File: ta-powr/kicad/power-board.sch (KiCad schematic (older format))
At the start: 7 parts, among them J1 PinSocket_16, J2 PinSocket_16, J3 PinSocket_4, J4 PinSocket_4, J5 PinSocket_4, J6 PinSocket_4, J7 MountingHole

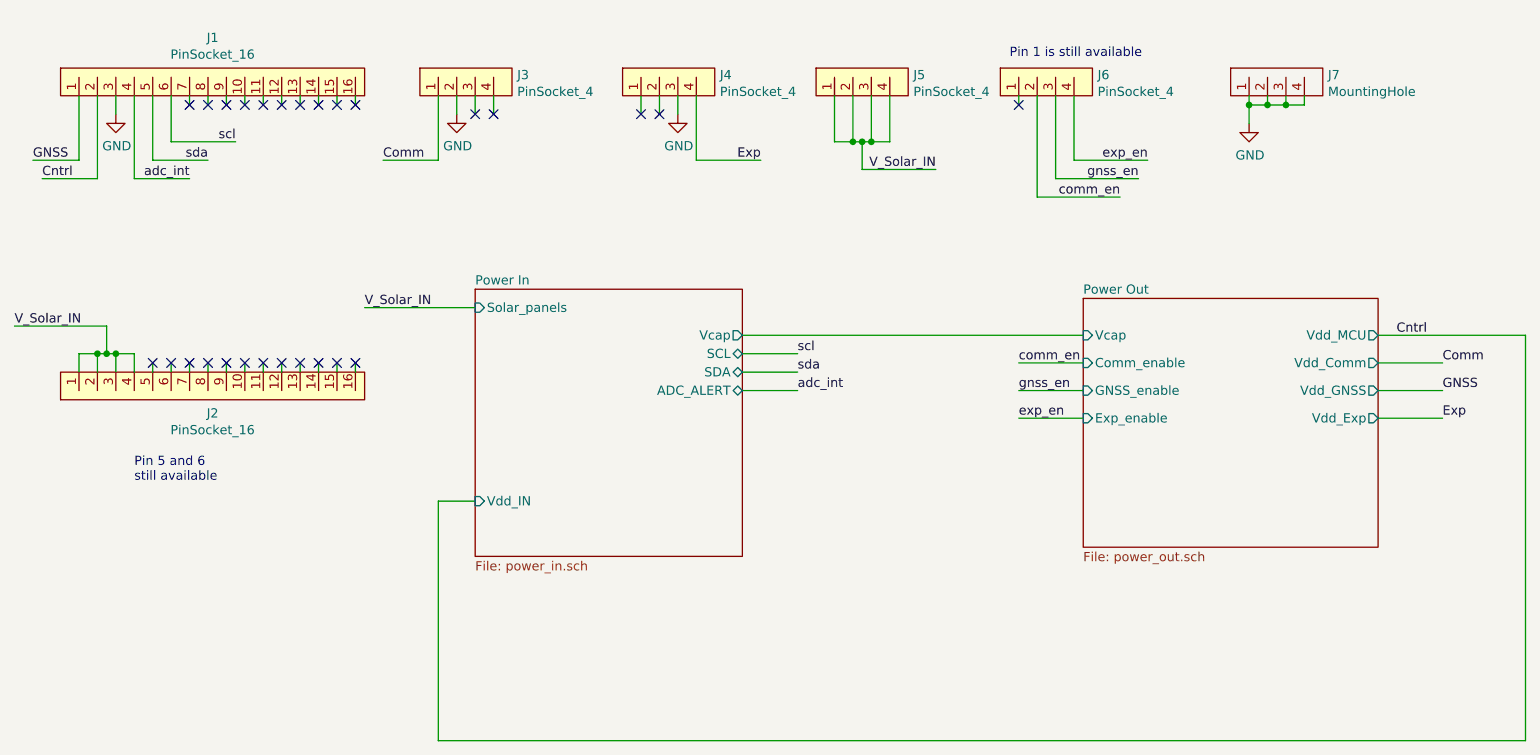
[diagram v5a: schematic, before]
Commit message: layout redone after pinout changes
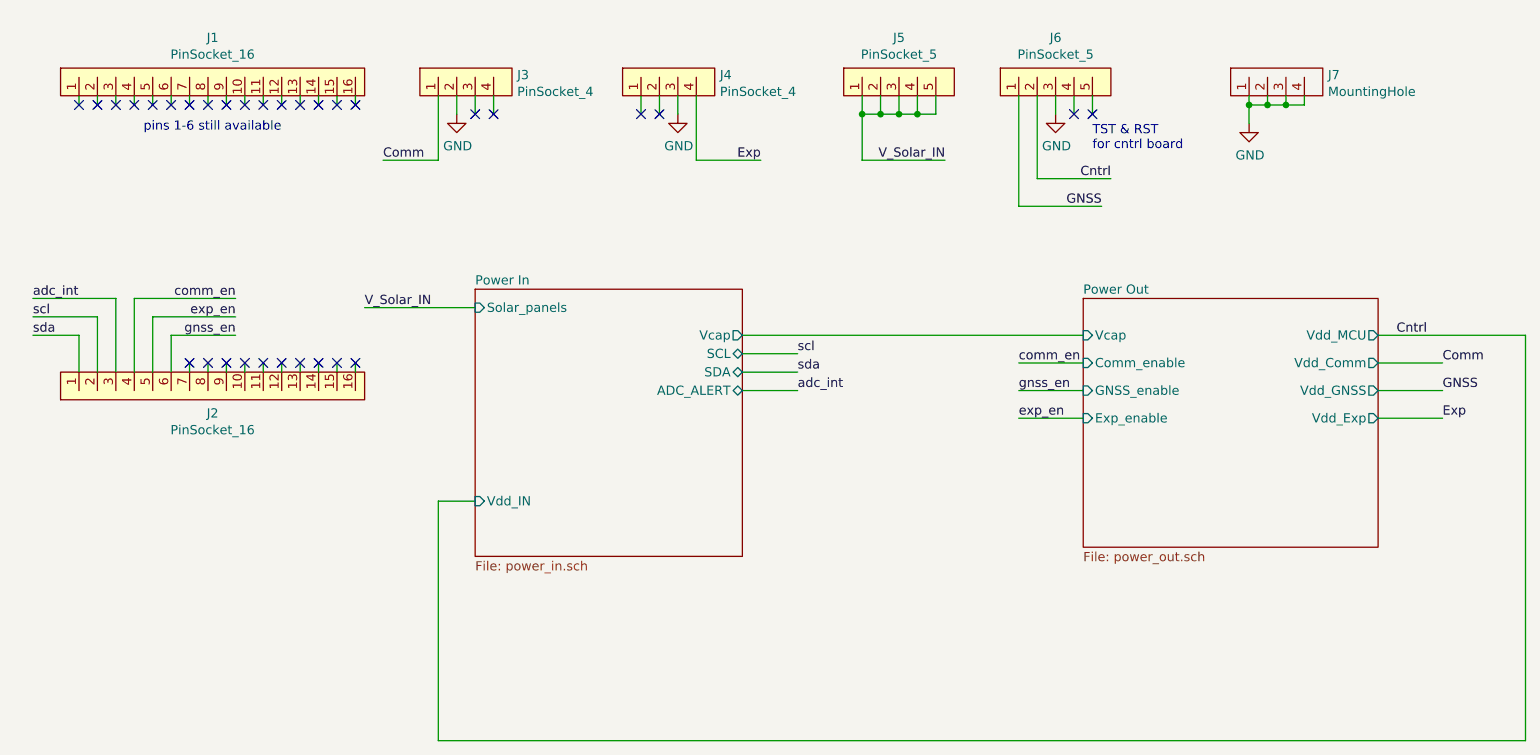
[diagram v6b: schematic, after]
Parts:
- removed J5, J6: PinSocket_4, ta-powr:PinSocket_1x4_TartanArtibeus_pwr_cpy, symbol power-board:PinSocket_4
- added J5: PinSocket_5, ta-powr:PinSocket_1x5_left_TartanArtibeus, symbol power-board:PinSocket_5
- added J6: PinSocket_5, ta-powr:PinSocket_1x5_right_TartanArtibeus, symbol power-board:PinSocket_5
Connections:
- net Cntrl: now also J6.2; no longer J1.2
- net GND: now also J6.3; no longer J1.3
- net GNSS: now also J6.1; no longer J1.1
- net V_Solar_IN: now also J5.1, J5.2, J5.3, J5.4, J5.5; no longer J2.1, J2.2, J2.3, J2.4
- net adc_int: now also J2.3; no longer J1.4
- net comm_en: now also J2.4
- net exp_en: now also J2.5
- net gnss_en: now also J2.6
- net scl: now also J2.2; no longer J1.6
- net sda: now also J2.1; no longer J1.5
- no-connect marks 27 -> 32
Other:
- note added: "TST & RST \nfor cntrl board"
- note added: "pins 1-6 still available"
- note removed: "Pin 1 is still available"
- note removed: "Pin 5 and 6\nstill available"
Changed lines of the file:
@@
-$EndComp
-$Comp
-L power-board:PinSocket_4 J5
-U 1 1 5F0EB25D
-P 5500 1150
-F 0 "J5" H 5778 1263 50  0000 L CNN
-F 1 "PinSocket_4" H 5778 1172 50  0000 L CNN
-F 2 "ta-powr:PinSocket_1x4_TartanArtibeus_pwr_cpy" H 5450 1150 50  0001 C CNN
-F 3 "" H 5450 1150 50  0001 C CNN
-	1    5500 1150
-	1    0    0    -1
-$EndComp
-$Comp
-L power-board:PinSocket_4 J6
-U 1 1 5F0EB733
-P 6500 1150
-F 0 "J6" H 6778 1263 50  0000 L CNN
-F 1 "PinSocket_4" H 6778 1172 50  0000 L CNN
-F 2 "ta-powr:PinSocket_1x4_TartanArtibeus_pwr_cpy" H 6450 1150 50  0001 C CNN
-F 3 "" H 6450 1150 50  0001 C CNN
-	1    6500 1150
-	1    0    0    -1
 $EndComp
 $Comp
@@
 	4400 1150 4400 1250
 Wire Wire Line
-	5350 1150 5350 1400
-Wire Wire Line
-	5350 1400 5450 1400
-Wire Wire Line
-	5650 1400 5650 1150
-Wire Wire Line
-	5450 1150 5450 1400
-Connection ~ 5450 1400
-Wire Wire Line
-	5450 1400 5500 1400
-Wire Wire Line
-	5550 1150 5550 1400
-Connection ~ 5550 1400
-Wire Wire Line
-	5550 1400 5650 1400
-Wire Wire Line
-	5500 1400 5500 1550
-Connection ~ 5500 1400
-Wire Wire Line
-	5500 1400 5550 1400
-Text Label 5900 1550 2    50   ~ 0
-V_Solar_IN
-Wire Wire Line
-	1250 2650 1250 2550
-Wire Wire Line
-	1250 2550 1350 2550
-Wire Wire Line
-	1550 2550 1550 2650
-Wire Wire Line
-	1450 2650 1450 2550
-Connection ~ 1450 2550
-Wire Wire Line
-	1450 2550 1550 2550
-Wire Wire Line
-	1350 2650 1350 2550
-Connection ~ 1350 2550
-Wire Wire Line
-	1350 2550 1400 2550
-Wire Wire Line
-	1400 2550 1400 2400
-Connection ~ 1400 2550
-Wire Wire Line
-	1400 2550 1450 2550
-Text Label 900  2400 0    50   ~ 0
-V_Solar_IN
-Wire Wire Line
-	900  2400 1400 2400
-Wire Wire Line
 	2800 2300 3400 2300
 Text Label 2800 2300 0    50   ~ 0
@@
 Cntrl
 Wire Wire Line
-	6650 1150 6650 1500
-Wire Wire Line
-	6650 1500 7050 1500
-Text Label 1050 1600 0    50   ~ 0
-Cntrl
-Wire Wire Line
 	4850 2550 5150 2550
 Wire Wire Line
@@
 Text Label 5150 2650 0    50   ~ 0
 sda
-Text Label 2100 1400 2    50   ~ 0
-scl
-Text Label 1950 1500 2    50   ~ 0
-sda
 Wire Wire Line
 	4850 2750 5150 2750
@@
 Wire Wire Line
 	6350 2900 6700 2900
-Wire Wire Line
-	5500 1550 5900 1550
-Wire Wire Line
-	1750 1150 1750 1400
-Wire Wire Line
-	1650 1150 1650 1500
-Wire Wire Line
-	1650 1500 1950 1500
-Wire Wire Line
-	1550 1150 1550 1600
-Text Label 1850 1600 2    50   ~ 0
+$Comp
+L power-board:PinSocket_5 J5
+U 1 1 5F12A0FB
+P 5700 1150
+F 0 "J5" H 5700 1465 50  0000 C CNN
+F 1 "PinSocket_5" H 5700 1374 50  0000 C CNN
+F 2 "ta-powr:PinSocket_1x5_left_TartanArtibeus" H 5600 1150 50  0001 C CNN
+F 3 "" H 5600 1150 50  0001 C CNN
+	1    5700 1150
+	1    0    0    -1
+$EndComp
+Wire Wire Line
+	5500 1150 5500 1250
+Wire Wire Line
+	5500 1250 5600 1250
+Wire Wire Line
+	5900 1250 5900 1150
+Wire Wire Line
+	5600 1150 5600 1250
+Connection ~ 5600 1250
+Wire Wire Line
+	5600 1250 5700 1250
+Wire Wire Line
+	5700 1150 5700 1250
+Connection ~ 5700 1250
+Wire Wire Line
+	5700 1250 5800 1250
+Wire Wire Line
+	5800 1150 5800 1250
+Connection ~ 5800 1250
+Wire Wire Line
+	5800 1250 5900 1250
+Wire Wire Line
+	5500 1250 5500 1500
+Connection ~ 5500 1250
+Text Label 5950 1500 2    50   ~ 0
+V_Solar_IN
+Wire Wire Line
+	5500 1500 5950 1500
+NoConn ~ 6750 1250
+NoConn ~ 6650 1250
+Wire Wire Line
+	6650 1150 6650 1250
+Wire Wire Line
+	6750 1150 6750 1250
+Text Notes 6750 1450 0    50   ~ 0
+TST & RST \nfor cntrl board
+$Comp
+L power:GND #PWR?
+U 1 1 5F138D11
+P 6550 1250
+AR Path="/5EF1389E/5F138D11" Ref="#PWR?"  Part="1"
+AR Path="/5F138D11" Ref="#PWR024"  Part="1"
+F 0 "#PWR024" H 6550 1000 50  0001 C CNN
+F 1 "GND" H 6555 1077 50  0000 C CNN
+F 2 "" H 6550 1250 50  0001 C CNN
+F 3 "" H 6550 1250 50  0001 C CNN
+	1    6550 1250
+	1    0    0    -1
+$EndComp
+Wire Wire Line
+	6550 1150 6550 1250
+Wire Wire Line
+	6450 1600 6850 1600
+Wire Wire Line
+	6450 1150 6450 1600
+Text Label 6850 1600 2    50   ~ 0
+Cntrl
+Wire Wire Line
+	1750 2650 1750 2450
+Wire Wire Line
+	1750 2450 2100 2450
+Wire Wire Line
+	1650 2350 2100 2350
+Wire Wire Line
+	1650 2350 1650 2650
+Wire Wire Line
+	1550 2650 1550 2250
+Wire Wire Line
+	1550 2250 2100 2250
+Text Label 2100 2250 2    50   ~ 0
+comm_en
+Text Label 2100 2350 2    50   ~ 0
+exp_en
+Text Label 2100 2450 2    50   ~ 0
+gnss_en
+Wire Wire Line
+	1250 2450 1250 2650
+Wire Wire Line
+	1250 2450 1000 2450
+Wire Wire Line
+	1350 2650 1350 2350
+Wire Wire Line
+	1350 2350 1000 2350
+Wire Wire Line
+	1450 2650 1450 2250
+Wire Wire Line
+	1450 2250 1000 2250
+Text Label 1000 2350 0    50   ~ 0
+scl
+Text Label 1000 2450 0    50   ~ 0
+sda
+Text Label 1000 2250 0    50   ~ 0
 adc_int
-Text Label 6900 1700 2    50   ~ 0
-comm_en
-Wire Wire Line
-	1750 1400 2100 1400
-Text Label 7000 1600 2    50   ~ 0
-gnss_en
-Text Label 7050 1500 2    50   ~ 0
-exp_en
-Wire Wire Line
-	1550 1600 1850 1600
-Text Label 1000 1500 0    50   ~ 0
+Text Notes 1600 1350 0    50   ~ 0
+pins 1-6 still available
+NoConn ~ 1750 1200
+NoConn ~ 1650 1200
+NoConn ~ 1550 1200
+NoConn ~ 1450 1200
+NoConn ~ 1350 1200
+Wire Wire Line
+	1350 1150 1350 1200
+Wire Wire Line
+	1450 1150 1450 1200
+Wire Wire Line
+	1550 1150 1550 1200
+Wire Wire Line
+	1650 1150 1650 1200
+Wire Wire Line
+	1750 1150 1750 1200
+NoConn ~ 1250 1200
+Wire Wire Line
+	1250 1150 1250 1200
+$Comp
+L power-board:PinSocket_5 J6
+U 1 1 5F0FE717
+P 6550 1150
+F 0 "J6" H 6550 1465 50  0000 C CNN
+F 1 "PinSocket_5" H 6550 1374 50  0000 C CNN
+F 2 "ta-powr:PinSocket_1x5_right_TartanArtibeus" H 6450 1150 50  0001 C CNN
+F 3 "" H 6450 1150 50  0001 C CNN
+	1    6550 1150
+	1    0    0    -1
+$EndComp
+Wire Wire Line
+	6350 1150 6350 1750
+Wire Wire Line
+	6350 1750 6800 1750
+Text Label 6800 1750 2    50   ~ 0
 GNSS
-$Comp
-L power:GND #PWR?
-U 1 1 5F120FFB
-P 1450 1250
-AR Path="/5EF1389E/5F120FFB" Ref="#PWR?"  Part="1"
-AR Path="/5F120FFB" Ref="#PWR0113"  Part="1"
-F 0 "#PWR0113" H 1450 1000 50  0001 C CNN
-F 1 "GND" H 1455 1077 50  0000 C CNN
-F 2 "" H 1450 1250 50  0001 C CNN
-F 3 "" H 1450 1250 50  0001 C CNN
-	1    1450 1250
-	1    0    0    -1
-$EndComp
-Wire Wire Line
-	1450 1150 1450 1250
-Wire Wire Line
-	1350 1150 1350 1600
-Wire Wire Line
-	1350 1600 1050 1600
-NoConn ~ 1650 2600
-Wire Wire Line
-	1650 2600 1650 2650
-Text Notes 1550 3250 0    50   ~ 0
-Pin 5 and 6\nstill available
-Text Notes 6300 950  0    50   ~ 0
-Pin 1 is still available
-Wire Wire Line
-	1250 1500 1000 1500
-Wire Wire Line
-	1250 1150 1250 1500
-Wire Wire Line
-	6550 1150 6550 1600
-Wire Wire Line
-	6450 1700 6900 1700
-Wire Wire Line
-	6450 1150 6450 1700
-Wire Wire Line
-	6550 1600 7000 1600
-NoConn ~ 6350 1200
-Wire Wire Line
-	6350 1150 6350 1200
-NoConn ~ 1750 2600
-Wire Wire Line
-	1750 2600 1750 2650
 $EndSCHEMATC

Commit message: Added all wires except for GND connections
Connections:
- net comm_en: now also J2.5; no longer J2.4
- net exp_en: now also J2.4; no longer J2.5
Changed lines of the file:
@@
 Wire Wire Line
 	1550 2250 2100 2250
+Text Label 2100 2350 2    50   ~ 0
+comm_en
 Text Label 2100 2250 2    50   ~ 0
-comm_en
-Text Label 2100 2350 2    50   ~ 0
 exp_en
 Text Label 2100 2450 2    50   ~ 0
@@
 	1250 2450 1250 2650
 Wire Wire Line
-	1250 2450 1000 2450
-Wire Wire Line
 	1350 2650 1350 2350
 Wire Wire Line
@@
 Wire Wire Line
 	1450 2650 1450 2250
-Wire Wire Line
-	1450 2250 1000 2250
 Text Label 1000 2350 0    50   ~ 0
 scl
-Text Label 1000 2450 0    50   ~ 0
+Text Label 900  2450 0    50   ~ 0
 sda
-Text Label 1000 2250 0    50   ~ 0
+Text Label 1150 2250 0    50   ~ 0
 adc_int
 Text Notes 1600 1350 0    50   ~ 0
@@
 Text Label 6800 1750 2    50   ~ 0
 GNSS
+Wire Wire Line
+	900  2450 1250 2450
+Wire Wire Line
+	1450 2250 1150 2250
 $EndSCHEMATC

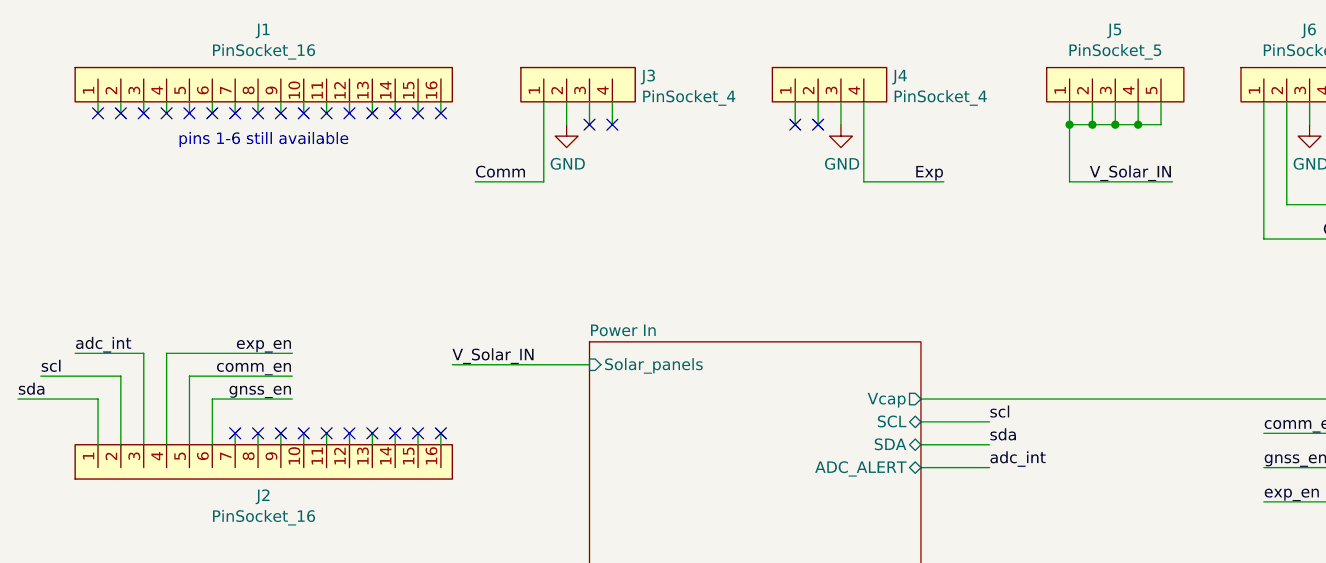
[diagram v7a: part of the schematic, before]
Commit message: fixes to power board after testing
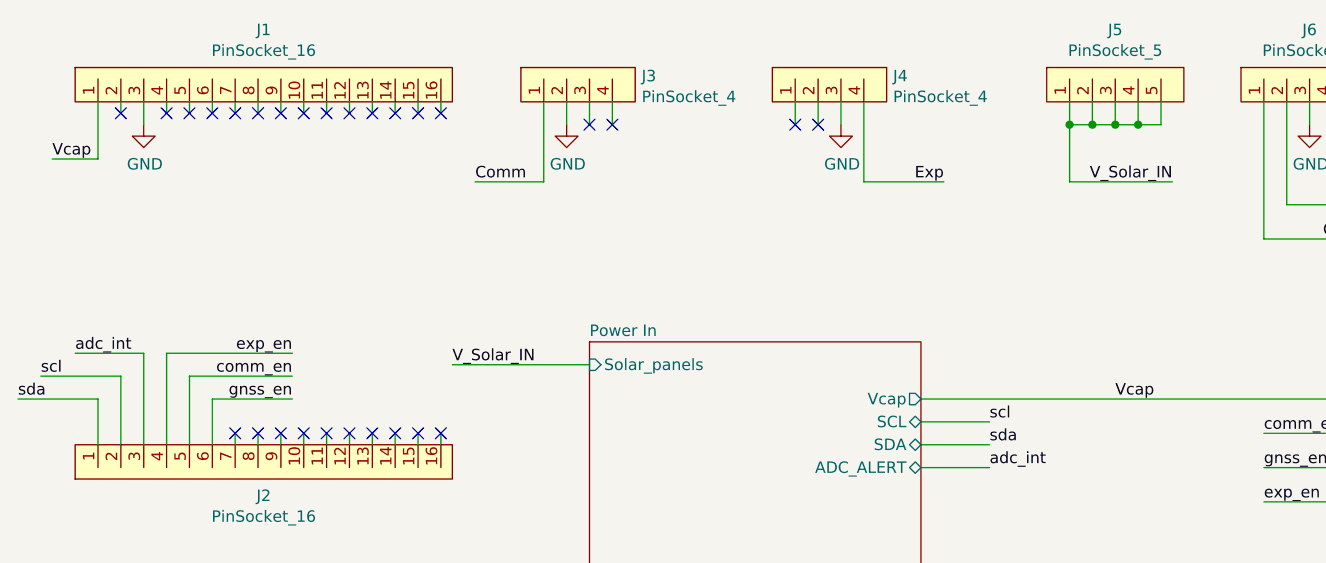
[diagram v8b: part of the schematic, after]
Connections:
- net GND: now also J1.3
- net Vcap: now reaches J1.1
- no-connect marks 32 -> 30
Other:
- note removed: "pins 1-6 still available"
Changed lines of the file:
@@
 Text Label 1150 2250 0    50   ~ 0
 adc_int
-Text Notes 1600 1350 0    50   ~ 0
-pins 1-6 still available
 NoConn ~ 1750 1200
 NoConn ~ 1650 1200
 NoConn ~ 1550 1200
-NoConn ~ 1450 1200
 NoConn ~ 1350 1200
 Wire Wire Line
 	1350 1150 1350 1200
-Wire Wire Line
-	1450 1150 1450 1200
 Wire Wire Line
 	1550 1150 1550 1200
@@
 Wire Wire Line
 	1750 1150 1750 1200
-NoConn ~ 1250 1200
-Wire Wire Line
-	1250 1150 1250 1200
 $Comp
 L power-board:PinSocket_5 J6
@@
 Wire Wire Line
 	1450 2250 1150 2250
+$Comp
+L power:GND #PWR?
+U 1 1 5F3EE243
+P 1450 1250
+AR Path="/5EF1389E/5F3EE243" Ref="#PWR?"  Part="1"
+AR Path="/5F3EE243" Ref="#PWR05"  Part="1"
+F 0 "#PWR05" H 1450 1000 50  0001 C CNN
+F 1 "GND" H 1455 1077 50  0000 C CNN
+F 2 "" H 1450 1250 50  0001 C CNN
+F 3 "" H 1450 1250 50  0001 C CNN
+	1    1450 1250
+	1    0    0    -1
+$EndComp
+Wire Wire Line
+	1450 1150 1450 1250
+Text Label 1050 1400 0    50   ~ 0
+Vcap
+Wire Wire Line
+	1250 1400 1050 1400
+Wire Wire Line
+	1250 1150 1250 1400
+Text Label 5700 2450 0    50   ~ 0
+Vcap
 $EndSCHEMATC
